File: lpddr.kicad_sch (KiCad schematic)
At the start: 63 parts, among them U1 MPFS250T-FCVG484, U11 MT53D512M32D2_WFBGA

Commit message: [#54016] Change 100nF to 0201 package
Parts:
- C190, C191, C192, C193, C208, C209, C210, C211, C212, C213, C214, C215, C216, C217, C218, C219, C232, C233, C234, C235, C236, C237, C238, C239, C240, C241: value C_100n_0402 -> C_100n_0201_25V; footprint antmicro-footprints:C_0402_1005Metric -> antmicro-footprints:C_0201; symbol antmicroCapacitors0402:C_100n_0402 -> antmicroCapacitorsmisc:C_100n_0201_25V; MPN GRM155R61H104KE14D -> C0603X5R1E104K030BB; Manufacturer Murata -> TDK; Voltage 50V -> 25V

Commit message: [#54899] Re-annotate components
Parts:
- renumbered C152 to C118, C153 to C119, C188 to C120, C189 to C121, C190 to C122, C191 to C123, C192 to C124, C193 to C125, C194 to C126, C195 to C127, C196 to C128, C197 to C129, C198 to C130, C199 to C131, C200 to C132, C201 to C133, C202 to C134, C203 to C135, C204 to C136, C205 to C137, C206 to C138, C207 to C139, C208 to C140, C209 to C141, C210 to C142, C211 to C143, C212 to C144, C213 to C145, C214 to C146, C215 to C147, C216 to C148, C217 to C149, C218 to C150, C219 to C151, C220 to C152, C221 to C153, C222 to C154, C223 to C155, C224 to C156, C225 to C157, C226 to C158, C227 to C159, C228 to C160, C229 to C161, C230 to C162, C231 to C163, C232 to C164, C233 to C165, C234 to C166, C235 to C167, C236 to C168, C237 to C169, C238 to C170, C239 to C171, C240 to C172, C241 to C173, C242 to C174, C243 to C175, R79 to R74, R80 to R75, R81 to R76, U11 to U12

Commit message: [#54899] Update symbols
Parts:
- U1: footprint antmicro-footprints:BGA-484_19x19mm_Layout22x22_P0.8mm_FCVG484 -> antmicro-footprints:BGA-484_19x19mm_Layout22x22_P0.8mm_MPFS250T-FCVG484
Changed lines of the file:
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@@
       (effects (font (size 1.27 1.27) (thickness 0.15)) (justify left bottom) hide)
     )
-    (property "Footprint" "antmicro-footprints:BGA-484_19x19mm_Layout22x22_P0.8mm_FCVG484" (at 167.64 76.2 0)
+    (property "Footprint" "antmicro-footprints:BGA-484_19x19mm_Layout22x22_P0.8mm_MPFS250T-FCVG484" (at 167.64 76.2 0)
       (effects (font (size 1.27 1.27) (thickness 0.15)) (justify left bottom) hide)
     )

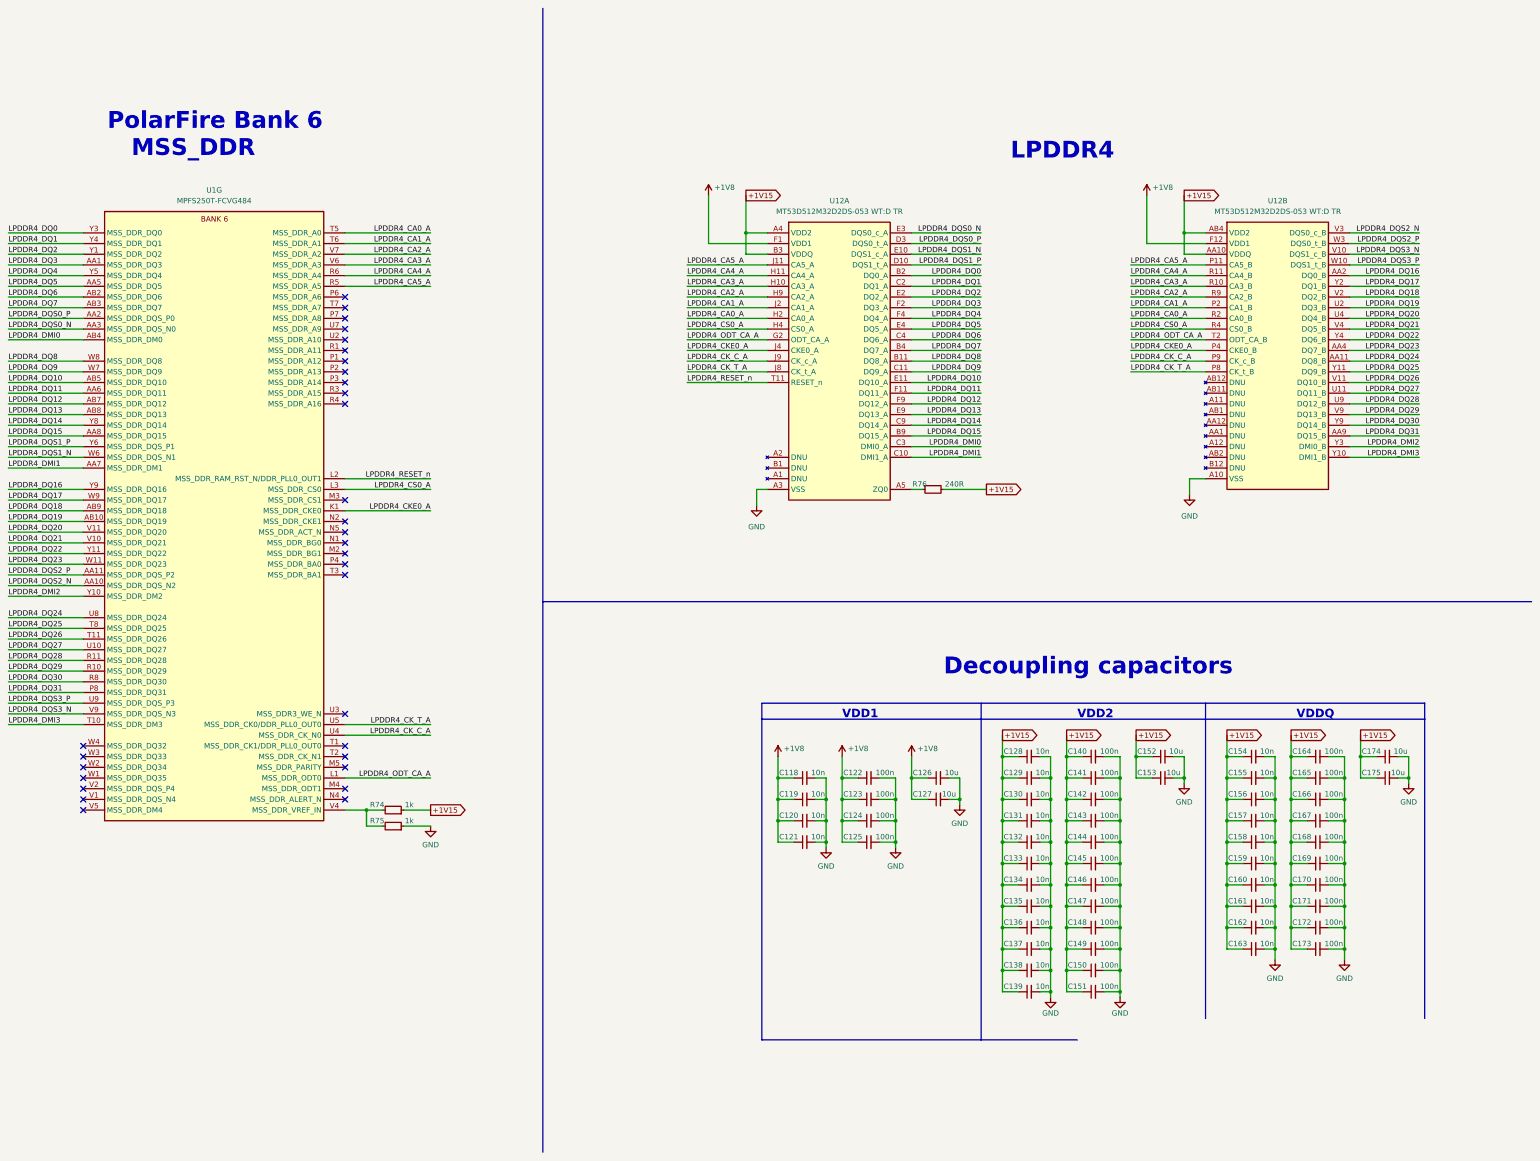
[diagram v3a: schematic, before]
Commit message: [#55288] Change LPDDR4 power supply to +1V1
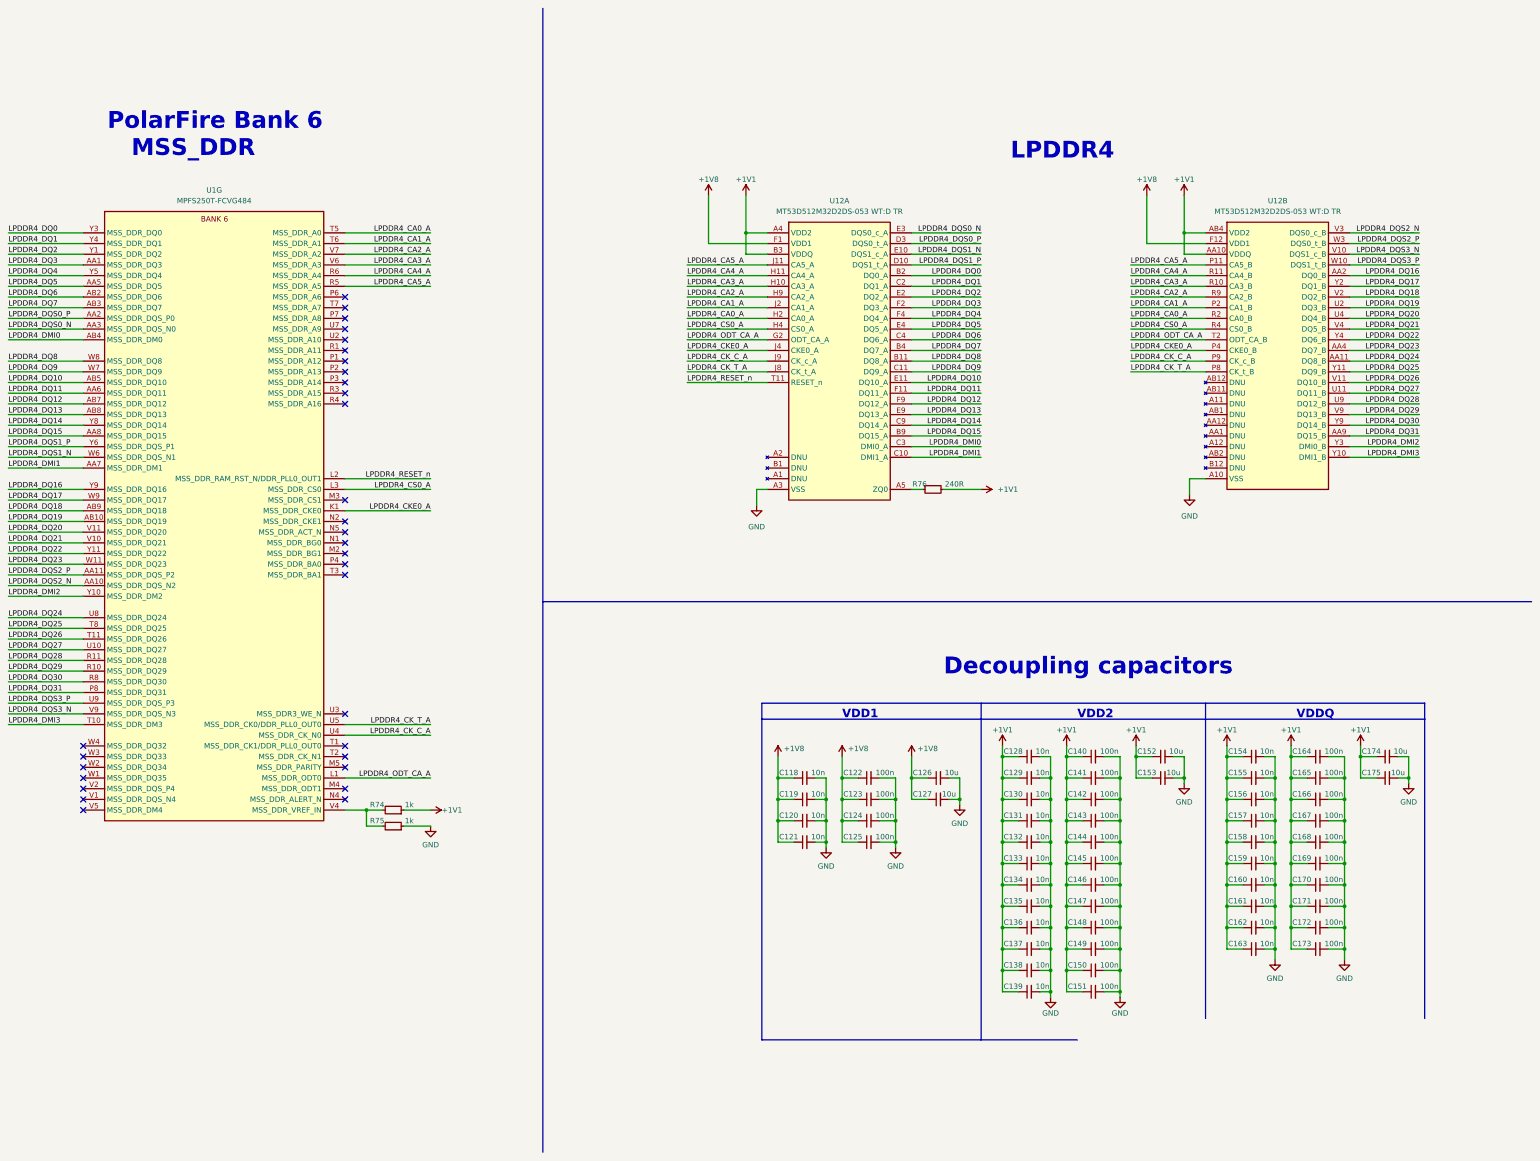
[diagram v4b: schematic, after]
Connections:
- net +1V15 renamed +1V1
